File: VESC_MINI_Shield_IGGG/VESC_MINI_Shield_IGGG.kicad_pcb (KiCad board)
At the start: 2 copper layers, 6 parts, among them J1 Sensor, J2 CAN, J3 CAN_MOLEX, J5 General, J6 NC

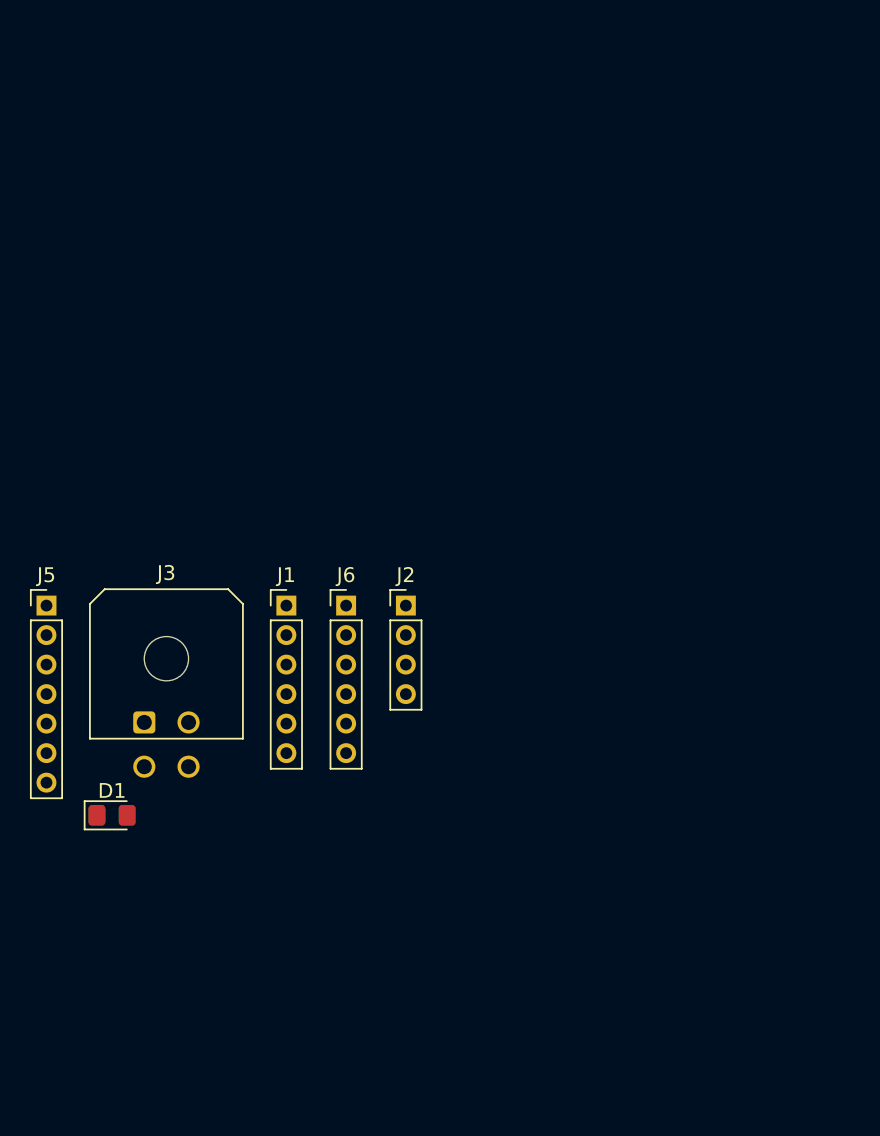
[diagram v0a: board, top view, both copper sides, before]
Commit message: vesc shield update
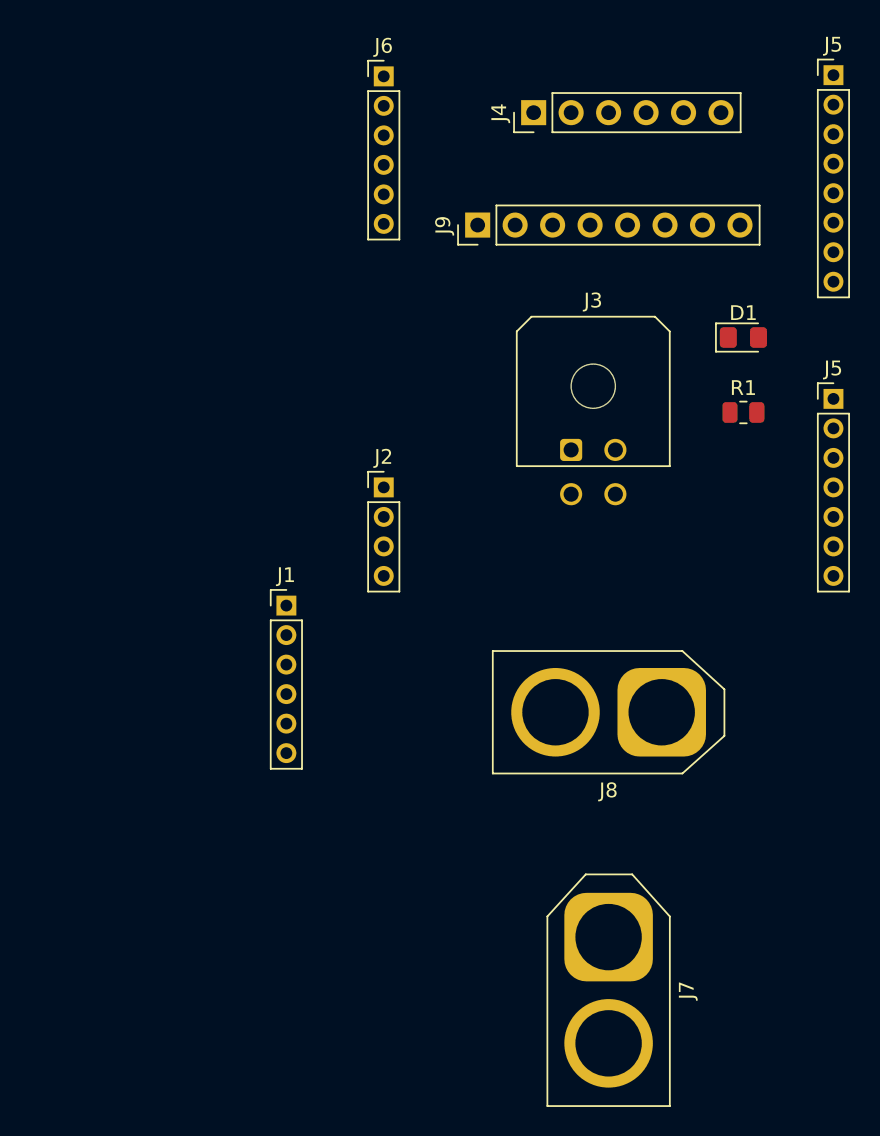
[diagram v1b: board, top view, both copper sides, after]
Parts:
- added J4: Encoder 1, Connector_PinHeader_2.54mm:PinHeader_1x06_P2.54mm_Vertical, F.Cu at (160.0, 38.1)
- added J5: Comm, Connector_PinHeader_2.00mm:PinHeader_1x08_P2.00mm_Vertical, F.Cu at (180.3, 35.6)
- added J7: XT60 IN, Connector_AMASS:AMASS_XT60-M_1x02_P7.20mm_Vertical, F.Cu at (165.1, 94.0)
- added J8: XT60 OUT, Connector_AMASS:AMASS_XT60-F_1x02_P7.20mm_Vertical, F.Cu at (168.7, 78.7)
- added J9: Encoder_out_port_8pin, Connector_PinHeader_2.54mm:PinHeader_1x08_P2.54mm_Vertical, F.Cu at (156.2, 45.7)
- added R1: 3.3K, Resistor_SMD:R_0805_2012Metric, F.Cu at (174.2, 58.4)
- moved J5 55.1 mm to (180.3, 57.5)
- moved D1 53.7 mm to (174.2, 53.3)
- moved J6 36.0 mm to (149.9, 35.6)
- moved J3 34.3 mm to (162.6, 61.0)
- moved J2 8.15 mm to (149.9, 63.5)
